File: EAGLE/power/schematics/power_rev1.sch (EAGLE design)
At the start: 9 parts

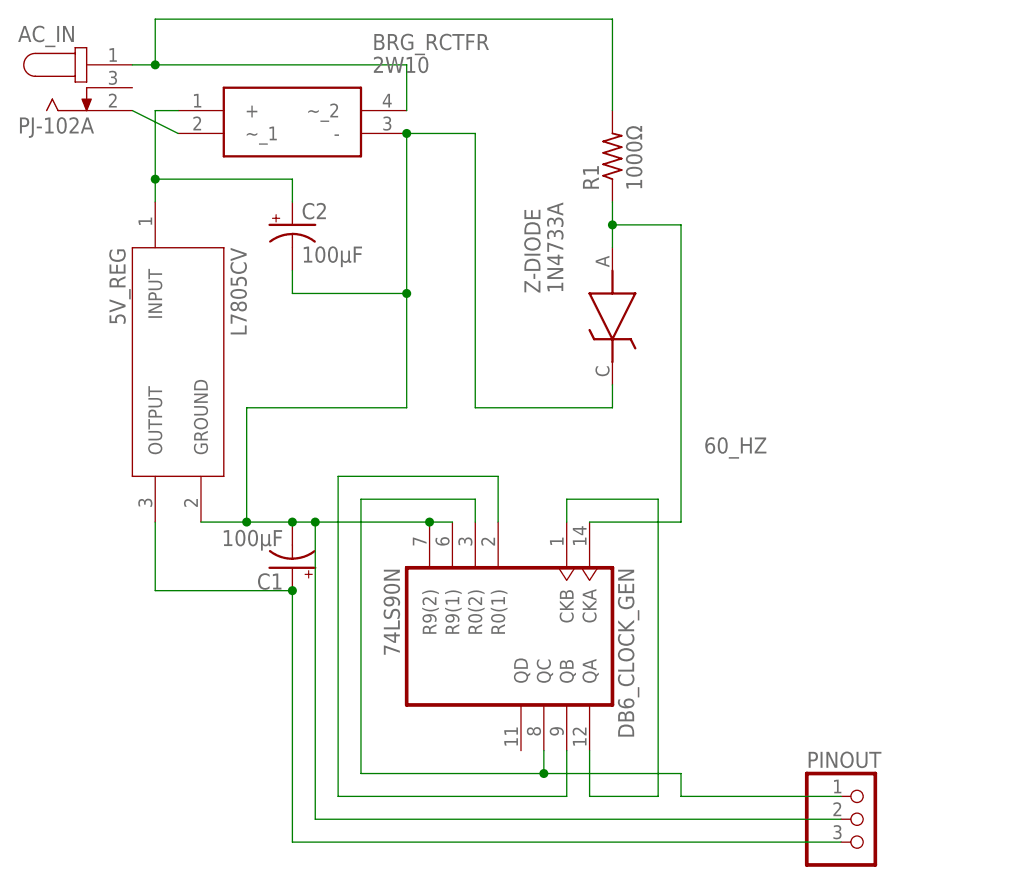
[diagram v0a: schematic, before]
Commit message: Update power_rev1.sch
Removedf pinout header for conversion to dbl
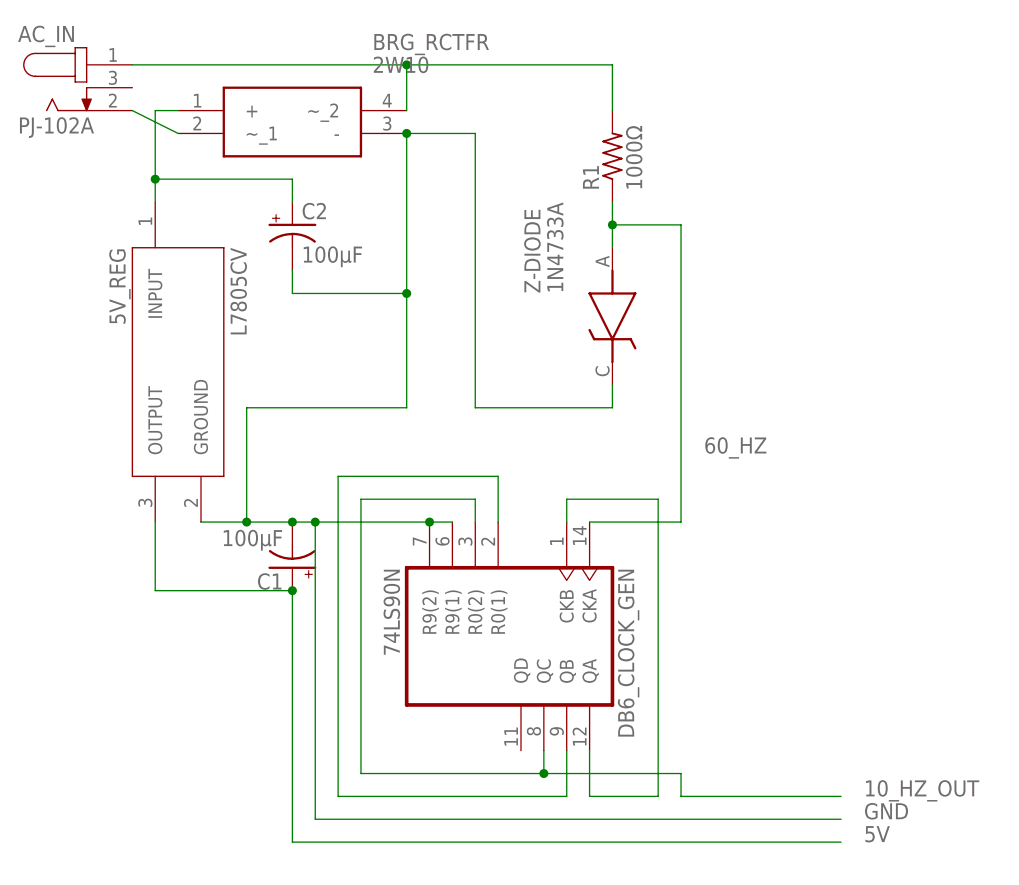
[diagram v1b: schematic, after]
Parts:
- removed PINOUT: (no value), pinhead:PINHD-1X3
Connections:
- removed net N$1: 5V_REG.GROUND, BRG_RCTFR.-, C1.-, C2.-, DB6_CLOCK_GENA.R9(1), DB6_CLOCK_GENA.R9(2), PINOUT.2, Z-DIODE.K
- removed net N$6: 5V_REG.OUTPUT, C1.+, PINOUT.3
- new net 5V: 5V_REG.OUTPUT, C1.+
- new net GND: 5V_REG.GROUND, BRG_RCTFR.-, C1.-, C2.-, DB6_CLOCK_GENA.R9(1), DB6_CLOCK_GENA.R9(2), Z-DIODE.K
- net 10_HZ_OUT: no longer PINOUT.1
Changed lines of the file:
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@@
 <?xml version="1.0" encoding="utf-8"?>
 <!DOCTYPE eagle SYSTEM "eagle.dtd">
-<eagle version="9.6.1">
+<eagle version="9.6.2">
 <drawing>
 <settings>
@@
 <grid distance="0.1" unitdist="inch" unit="inch" style="lines" multiple="1" display="no" altdistance="0.01" altunitdist="inch" altunit="inch"/>
 <layers>
-<layer number="1" name="Top" color="4" fill="1" visible="yes" active="no"/>
-<layer number="16" name="Bottom" color="1" fill="1" visible="yes" active="no"/>
-<layer number="17" name="Pads" color="2" fill="1" visible="yes" active="no"/>
-<layer number="18" name="Vias" color="2" fill="1" visible="yes" active="no"/>
-<layer number="19" name="Unrouted" color="6" fill="1" visible="yes" active="no"/>
-<layer number="20" name="Dimension" color="15" fill="1" visible="yes" active="no"/>
-<layer number="21" name="tPlace" color="7" fill="1" visible="yes" active="no"/>
-<layer number="22" name="bPlace" color="7" fill="1" visible="yes" active="no"/>
-<layer number="23" name="tOrigins" color="15" fill="1" visible="yes" active="no"/>
-<layer number="24" name="bOrigins" color="15" fill="1" visible="yes" active="no"/>
-<layer number="25" name="tNames" color="7" fill="1" visible="yes" active="no"/>
-<layer number="26" name="bNames" color="7" fill="1" visible="yes" active="no"/>
-<layer number="27" name="tValues" color="7" fill="1" visible="yes" active="no"/>
-<layer number="28" name="bValues" color="7" fill="1" visible="yes" active="no"/>
+<layer number="1" name="Top" color="4" fill="1" visible="no" active="no"/>
+<layer number="16" name="Bottom" color="1" fill="1" visible="no" active="no"/>
+<layer number="17" name="Pads" color="2" fill="1" visible="no" active="no"/>
+<layer number="18" name="Vias" color="2" fill="1" visible="no" active="no"/>
+<layer number="19" name="Unrouted" color="6" fill="1" visible="no" active="no"/>
+<layer number="20" name="Dimension" color="15" fill="1" visible="no" active="no"/>
+<layer number="21" name="tPlace" color="7" fill="1" visible="no" active="no"/>
+<layer number="22" name="bPlace" color="7" fill="1" visible="no" active="no"/>
+<layer number="23" name="tOrigins" color="15" fill="1" visible="no" active="no"/>
+<layer number="24" name="bOrigins" color="15" fill="1" visible="no" active="no"/>
+<layer number="25" name="tNames" color="7" fill="1" visible="no" active="no"/>
+<layer number="26" name="bNames" color="7" fill="1" visible="no" active="no"/>
+<layer number="27" name="tValues" color="7" fill="1" visible="no" active="no"/>
+<layer number="28" name="bValues" color="7" fill="1" visible="no" active="no"/>
 <layer number="29" name="tStop" color="7" fill="3" visible="no" active="no"/>
 <layer number="30" name="bStop" color="7" fill="6" visible="no" active="no"/>
@@
 <layer number="35" name="tGlue" color="7" fill="4" visible="no" active="no"/>
 <layer number="36" name="bGlue" color="7" fill="5" visible="no" active="no"/>
-<layer number="37" name="tTest" color="7" fill="1" visible="yes" active="no"/>
-<layer number="38" name="bTest" color="7" fill="1" visible="yes" active="no"/>
+<layer number="37" name="tTest" color="7" fill="1" visible="no" active="no"/>
+<layer number="38" name="bTest" color="7" fill="1" visible="no" active="no"/>
 <layer number="39" name="tKeepout" color="4" fill="11" visible="no" active="no"/>
 <layer number="40" name="bKeepout" color="1" fill="11" visible="no" active="no"/>
@@
 <layer number="44" name="Drills" color="7" fill="1" visible="no" active="no"/>
 <layer number="45" name="Holes" color="7" fill="1" visible="no" active="no"/>
-<layer number="46" name="Milling" color="3" fill="1" visible="yes" active="no"/>
-<layer number="47" name="Measures" color="7" fill="1" visible="yes" active="no"/>
-<layer number="48" name="Document" color="7" fill="1" visible="yes" active="no"/>
-<layer number="49" name="Reference" color="7" fill="1" visible="yes" active="no"/>
-<layer number="51" name="tDocu" color="7" fill="1" visible="yes" active="no"/>
-<layer number="52" name="bDocu" color="7" fill="1" visible="yes" active="no"/>
+<layer number="46" name="Milling" color="3" fill="1" visible="no" active="no"/>
+<layer number="47" name="Measures" color="7" fill="1" visible="no" active="no"/>
+<layer number="48" name="Document" color="7" fill="1" visible="no" active="no"/>
+<layer number="49" name="Reference" color="7" fill="1" visible="no" active="no"/>
+<layer number="51" name="tDocu" color="7" fill="1" visible="no" active="no"/>
+<layer number="52" name="bDocu" color="7" fill="1" visible="no" active="no"/>
 <layer number="88" name="SimResults" color="9" fill="1" visible="yes" active="yes"/>
 <layer number="89" name="SimProbes" color="9" fill="1" visible="yes" active="yes"/>
@@
 <part name="C2" library="rcl" library_urn="urn:adsk.eagle:library:334" deviceset="CPOL-US" device="E2.5-6" package3d_urn="urn:adsk.eagle:package:23349/1" value="100μF"/>
 <part name="DB6_CLOCK_GEN" library="74xx-us" library_urn="urn:adsk.eagle:library:88" deviceset="74*90" device="N" package3d_urn="urn:adsk.eagle:package:16407/2" technology="LS"/>
-<part name="PINOUT" library="pinhead" library_urn="urn:adsk.eagle:library:325" deviceset="PINHD-1X3" device="" package3d_urn="urn:adsk.eagle:package:22458/2"/>
 </parts>
 <sheets>
@@
 <attribute name="NAME" x="74.295" y="17.78" size="1.778" layer="95" rot="R270"/>
 <attribute name="VALUE" x="48.26" y="17.78" size="1.778" layer="96" rot="R270"/>
-</instance>
-<instance part="PINOUT" gate="A" x="101.6" y="-10.16" smashed="yes">
-<attribute name="NAME" x="95.25" y="-4.445" size="1.778" layer="95"/>
-<attribute name="VALUE" x="95.25" y="-17.78" size="1.778" layer="96"/>
 </instance>
 </instances>
@@
 </segment>
 </net>
-<net name="N$6" class="0">
+<net name="5V" class="0">
 <segment>
 <pinref part="5V_REG" gate="G$1" pin="OUTPUT"/>
@@
 <wire x1="38.1" y1="-12.7" x2="99.06" y2="-12.7" width="0.1524" layer="91"/>
 <junction x="38.1" y="15.24"/>
-<pinref part="PINOUT" gate="A" pin="3"/>
+<label x="101.6" y="-12.7" size="1.778" layer="95"/>
 </segment>
 </net>
@@
 <wire x1="66.04" y1="-5.08" x2="81.28" y2="-5.08" width="0.1524" layer="91"/>
 <junction x="66.04" y="-5.08"/>
-<pinref part="PINOUT" gate="A" pin="1"/>
 <wire x1="99.06" y1="-7.62" x2="81.28" y2="-7.62" width="0.1524" layer="91"/>
 <wire x1="81.28" y1="-7.62" x2="81.28" y2="-5.08" width="0.1524" layer="91"/>
+<label x="101.6" y="-7.62" size="1.778" layer="95"/>
 </segment>
 </net>
@@
 <net name="N$3" class="0">
 <segment>
-<pinref part="R1" gate="G$1" pin="2"/>
-<wire x1="73.66" y1="68.58" x2="73.66" y2="78.74" width="0.1524" layer="91"/>
 <pinref part="AC_IN" gate="G$1" pin="1"/>
 <pinref part="BRG_RCTFR" gate="G$1" pin="~_2"/>
-<wire x1="20.32" y1="73.66" x2="22.86" y2="73.66" width="0.1524" layer="91"/>
-<wire x1="22.86" y1="73.66" x2="50.8" y2="73.66" width="0.1524" layer="91"/>
+<wire x1="20.32" y1="73.66" x2="50.8" y2="73.66" width="0.1524" layer="91"/>
 <wire x1="50.8" y1="73.66" x2="50.8" y2="68.58" width="0.1524" layer="91"/>
-<wire x1="73.66" y1="78.74" x2="22.86" y2="78.74" width="0.1524" layer="91"/>
-<wire x1="22.86" y1="78.74" x2="22.86" y2="73.66" width="0.1524" layer="91"/>
-<junction x="22.86" y="73.66"/>
-</segment>
-</net>
-<net name="N$1" class="0">
+<pinref part="R1" gate="G$1" pin="2"/>
+<wire x1="73.66" y1="68.58" x2="73.66" y2="73.66" width="0.1524" layer="91"/>
+<wire x1="50.8" y1="73.66" x2="73.66" y2="73.66" width="0.1524" layer="91"/>
+<junction x="50.8" y="73.66"/>
+</segment>
+</net>
+<net name="GND" class="0">
 <segment>
 <pinref part="BRG_RCTFR" gate="G$1" pin="-"/>
@@
 <wire x1="40.64" y1="-10.16" x2="99.06" y2="-10.16" width="0.1524" layer="91"/>
 <junction x="40.64" y="22.86"/>
-<pinref part="PINOUT" gate="A" pin="2"/>
 <wire x1="50.8" y1="35.56" x2="33.02" y2="35.56" width="0.1524" layer="91"/>
 <wire x1="33.02" y1="35.56" x2="33.02" y2="22.86" width="0.1524" layer="91"/>
@@
 <junction x="50.8" y="66.04"/>
 <junction x="50.8" y="48.26"/>
-</segment>
-</net>
+<label x="101.6" y="-10.16" size="1.778" layer="95"/>
+</segment>
+</net>

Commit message: straightened net
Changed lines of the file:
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@@
 </busses>
 <nets>
-<net name="N$2" class="0">
-<segment>
-<pinref part="AC_IN" gate="G$1" pin="2"/>
-<pinref part="BRG_RCTFR" gate="G$1" pin="~_1"/>
-<wire x1="20.32" y1="68.58" x2="25.4" y2="66.04" width="0.1524" layer="91"/>
-</segment>
-</net>
 <net name="60_HZ" class="0">
 <segment>
@@
 </segment>
 </net>
+<net name="N$1" class="0">
+<segment>
+<pinref part="BRG_RCTFR" gate="G$1" pin="~_1"/>
+<pinref part="AC_IN" gate="G$1" pin="2"/>
+<wire x1="25.4" y1="66.04" x2="20.32" y2="66.04" width="0.1524" layer="91"/>
+<wire x1="20.32" y1="66.04" x2="20.32" y2="68.58" width="0.1524" layer="91"/>
+</segment>
+</net>
